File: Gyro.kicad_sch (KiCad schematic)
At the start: 5 parts, among them U4 MPU-6050

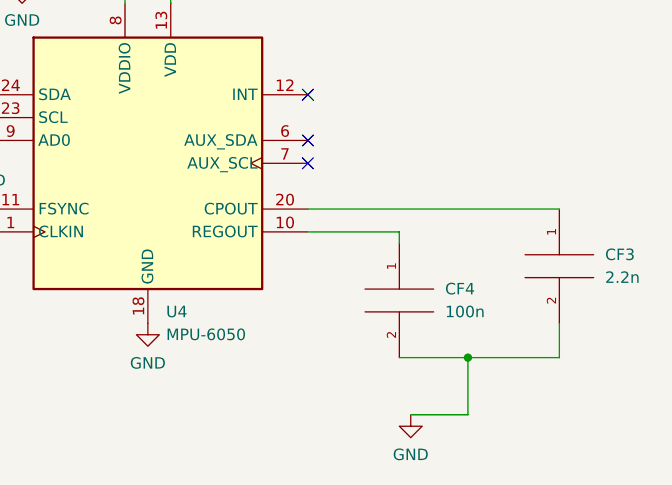
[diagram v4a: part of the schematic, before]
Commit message: Page settings changed. Added some testpoints. Some comments are made.
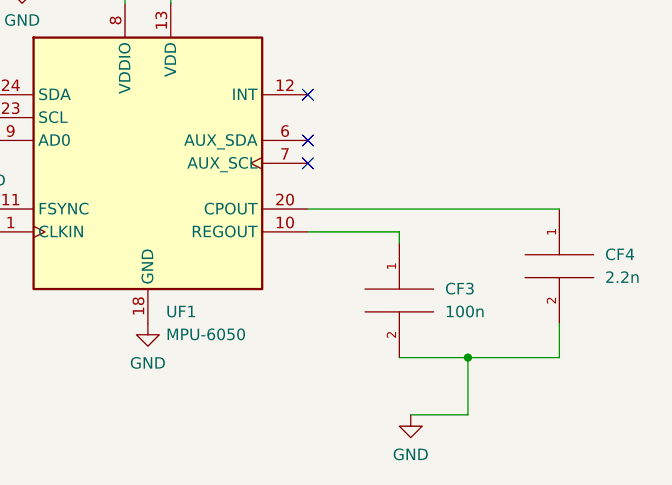
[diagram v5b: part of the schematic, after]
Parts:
- renumbered CF4 to CF3, CF3 to CF4, U4 to UF1
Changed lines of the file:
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@@
   (symbol (lib_id "pspice:C") (at 161.29 97.79 0) (unit 1)
     (in_bom yes) (on_board yes) (fields_autoplaced)
-    (property "Reference" "CF4" (id 0) (at 166.37 96.5199 0)
+    (property "Reference" "CF3" (id 0) (at 166.37 96.5199 0)
       (effects (font (size 1.27 1.27)) (justify left))
     )
@@
   (symbol (lib_id "upsat-comms-hardware:GND") (at 162.56 110.49 0) (unit 1)
     (in_bom yes) (on_board yes) (fields_autoplaced)
-    (property "Reference" "#PWR069" (id 0) (at 162.56 116.84 0)
+    (property "Reference" "#PWR082" (id 0) (at 162.56 116.84 0)
       (effects (font (size 1.27 1.27)) hide)
     )
@@
   (symbol (lib_id "upsat-comms-hardware:GND") (at 113.03 93.98 0) (unit 1)
     (in_bom yes) (on_board yes) (fields_autoplaced)
-    (property "Reference" "#PWR067" (id 0) (at 113.03 100.33 0)
+    (property "Reference" "#PWR078" (id 0) (at 113.03 100.33 0)
       (effects (font (size 1.27 1.27)) hide)
     )
@@
   (symbol (lib_id "upsat-comms-hardware:GND") (at 115.57 80.01 0) (unit 1)
     (in_bom yes) (on_board yes) (fields_autoplaced)
-    (property "Reference" "#PWR066" (id 0) (at 115.57 86.36 0)
+    (property "Reference" "#PWR079" (id 0) (at 115.57 86.36 0)
       (effects (font (size 1.27 1.27)) hide)
     )
@@
   (symbol (lib_id "pspice:C") (at 179.07 93.98 0) (unit 1)
     (in_bom yes) (on_board yes) (fields_autoplaced)
-    (property "Reference" "CF3" (id 0) (at 184.15 92.7099 0)
+    (property "Reference" "CF4" (id 0) (at 184.15 92.7099 0)
       (effects (font (size 1.27 1.27)) (justify left))
     )
@@
   (symbol (lib_id "upsat-comms-hardware:GND") (at 119.38 62.23 0) (unit 1)
     (in_bom yes) (on_board yes) (fields_autoplaced)
-    (property "Reference" "#PWR065" (id 0) (at 119.38 68.58 0)
+    (property "Reference" "#PWR080" (id 0) (at 119.38 68.58 0)
       (effects (font (size 1.27 1.27)) hide)
     )
@@
   (symbol (lib_id "upsat-comms-hardware:GND") (at 133.35 100.33 0) (unit 1)
     (in_bom yes) (on_board yes) (fields_autoplaced)
-    (property "Reference" "#PWR068" (id 0) (at 133.35 106.68 0)
+    (property "Reference" "#PWR081" (id 0) (at 133.35 106.68 0)
       (effects (font (size 1.27 1.27)) hide)
     )
@@
   (symbol (lib_id "Sensor_Motion:MPU-6050") (at 133.35 82.55 0) (unit 1)
     (in_bom yes) (on_board yes) (fields_autoplaced)
-    (property "Reference" "U4" (id 0) (at 135.3694 99.06 0)
+    (property "Reference" "UF1" (id 0) (at 135.3694 99.06 0)
       (effects (font (size 1.27 1.27)) (justify left))
     )

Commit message: I2C lines are pulled up
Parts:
- CF1, CF2, CF3, CF4: footprint (none) -> Capacitor_SMD:C_0603_1608Metric
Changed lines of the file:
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@@
       (effects (font (size 1.27 1.27)) (justify left))
     )
-    (property "Footprint" "" (id 2) (at 161.29 97.79 0)
+    (property "Footprint" "Capacitor_SMD:C_0603_1608Metric" (id 2) (at 161.29 97.79 0)
       (effects (font (size 1.27 1.27)) hide)
     )
@@
       (effects (font (size 1.27 1.27)) (justify left))
     )
-    (property "Footprint" "" (id 2) (at 114.3 53.34 0)
+    (property "Footprint" "Capacitor_SMD:C_0603_1608Metric" (id 2) (at 114.3 53.34 0)
       (effects (font (size 1.27 1.27)) hide)
     )
@@
   (symbol (lib_id "upsat-comms-hardware:GND") (at 162.56 110.49 0) (unit 1)
     (in_bom yes) (on_board yes) (fields_autoplaced)
-    (property "Reference" "#PWR082" (id 0) (at 162.56 116.84 0)
+    (property "Reference" "#PWR083" (id 0) (at 162.56 116.84 0)
       (effects (font (size 1.27 1.27)) hide)
     )
@@
       (effects (font (size 1.27 1.27)) (justify left))
     )
-    (property "Footprint" "" (id 2) (at 124.46 53.34 0)
+    (property "Footprint" "Capacitor_SMD:C_0603_1608Metric" (id 2) (at 124.46 53.34 0)
       (effects (font (size 1.27 1.27)) hide)
     )
@@
   (symbol (lib_id "upsat-comms-hardware:GND") (at 113.03 93.98 0) (unit 1)
     (in_bom yes) (on_board yes) (fields_autoplaced)
-    (property "Reference" "#PWR078" (id 0) (at 113.03 100.33 0)
+    (property "Reference" "#PWR079" (id 0) (at 113.03 100.33 0)
       (effects (font (size 1.27 1.27)) hide)
     )
@@
   (symbol (lib_id "upsat-comms-hardware:GND") (at 115.57 80.01 0) (unit 1)
     (in_bom yes) (on_board yes) (fields_autoplaced)
-    (property "Reference" "#PWR079" (id 0) (at 115.57 86.36 0)
+    (property "Reference" "#PWR080" (id 0) (at 115.57 86.36 0)
       (effects (font (size 1.27 1.27)) hide)
     )
@@
       (effects (font (size 1.27 1.27)) (justify left))
     )
-    (property "Footprint" "" (id 2) (at 179.07 93.98 0)
+    (property "Footprint" "Capacitor_SMD:C_0603_1608Metric" (id 2) (at 179.07 93.98 0)
       (effects (font (size 1.27 1.27)) hide)
     )
@@
   (symbol (lib_id "upsat-comms-hardware:GND") (at 119.38 62.23 0) (unit 1)
     (in_bom yes) (on_board yes) (fields_autoplaced)
-    (property "Reference" "#PWR080" (id 0) (at 119.38 68.58 0)
+    (property "Reference" "#PWR081" (id 0) (at 119.38 68.58 0)
       (effects (font (size 1.27 1.27)) hide)
     )
@@
   (symbol (lib_id "upsat-comms-hardware:GND") (at 133.35 100.33 0) (unit 1)
     (in_bom yes) (on_board yes) (fields_autoplaced)
-    (property "Reference" "#PWR081" (id 0) (at 133.35 106.68 0)
+    (property "Reference" "#PWR082" (id 0) (at 133.35 106.68 0)
       (effects (font (size 1.27 1.27)) hide)
     )

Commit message: Final Schematic
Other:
- moved on the sheet: CF1, CF2, CF3, CF4, UF1

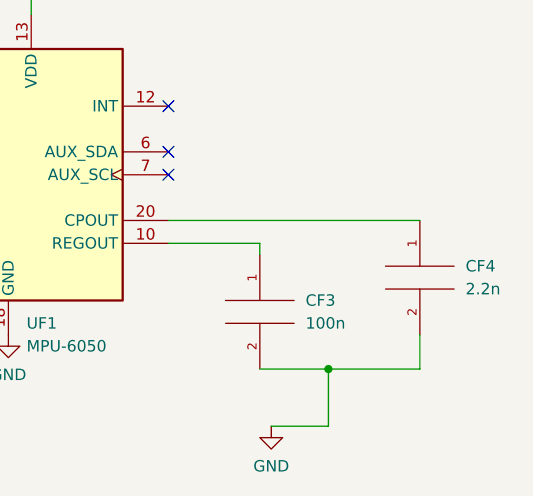
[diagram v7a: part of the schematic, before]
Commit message: MCU circuitry forgot LOL
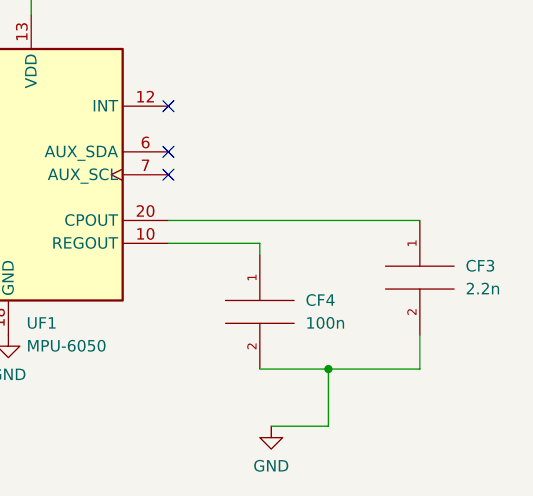
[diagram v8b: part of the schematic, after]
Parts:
- renumbered CF4 to CF3, CF3 to CF4
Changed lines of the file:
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@@
   (symbol (lib_id "pspice:C") (at 169.672 111.76 0) (unit 1)
     (in_bom yes) (on_board yes) (fields_autoplaced)
-    (property "Reference" "CF3" (id 0) (at 174.752 110.4899 0)
+    (property "Reference" "CF4" (id 0) (at 174.752 110.4899 0)
       (effects (font (size 1.27 1.27)) (justify left))
     )
@@
   (symbol (lib_id "upsat-comms-hardware:GND") (at 170.942 124.46 0) (unit 1)
     (in_bom yes) (on_board yes) (fields_autoplaced)
-    (property "Reference" "#PWR083" (id 0) (at 170.942 130.81 0)
+    (property "Reference" "#PWR090" (id 0) (at 170.942 130.81 0)
       (effects (font (size 1.27 1.27)) hide)
     )
@@
   (symbol (lib_id "upsat-comms-hardware:GND") (at 121.412 107.95 0) (unit 1)
     (in_bom yes) (on_board yes) (fields_autoplaced)
-    (property "Reference" "#PWR079" (id 0) (at 121.412 114.3 0)
+    (property "Reference" "#PWR088" (id 0) (at 121.412 114.3 0)
       (effects (font (size 1.27 1.27)) hide)
     )
@@
   (symbol (lib_id "upsat-comms-hardware:GND") (at 123.952 93.98 0) (unit 1)
     (in_bom yes) (on_board yes) (fields_autoplaced)
-    (property "Reference" "#PWR080" (id 0) (at 123.952 100.33 0)
+    (property "Reference" "#PWR087" (id 0) (at 123.952 100.33 0)
       (effects (font (size 1.27 1.27)) hide)
     )
@@
   (symbol (lib_id "pspice:C") (at 187.452 107.95 0) (unit 1)
     (in_bom yes) (on_board yes) (fields_autoplaced)
-    (property "Reference" "CF4" (id 0) (at 192.532 106.6799 0)
+    (property "Reference" "CF3" (id 0) (at 192.532 106.6799 0)
       (effects (font (size 1.27 1.27)) (justify left))
     )
@@
   (symbol (lib_id "upsat-comms-hardware:GND") (at 127.762 76.2 0) (unit 1)
     (in_bom yes) (on_board yes) (fields_autoplaced)
-    (property "Reference" "#PWR081" (id 0) (at 127.762 82.55 0)
+    (property "Reference" "#PWR086" (id 0) (at 127.762 82.55 0)
       (effects (font (size 1.27 1.27)) hide)
     )
@@
   (symbol (lib_id "upsat-comms-hardware:GND") (at 141.732 114.3 0) (unit 1)
     (in_bom yes) (on_board yes) (fields_autoplaced)
-    (property "Reference" "#PWR082" (id 0) (at 141.732 120.65 0)
+    (property "Reference" "#PWR089" (id 0) (at 141.732 120.65 0)
       (effects (font (size 1.27 1.27)) hide)
     )
